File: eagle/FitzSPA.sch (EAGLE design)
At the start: 30 parts, among them U1 AD9200ARZ, U2 AD8129ARMZ, U3 VAT1-SMT

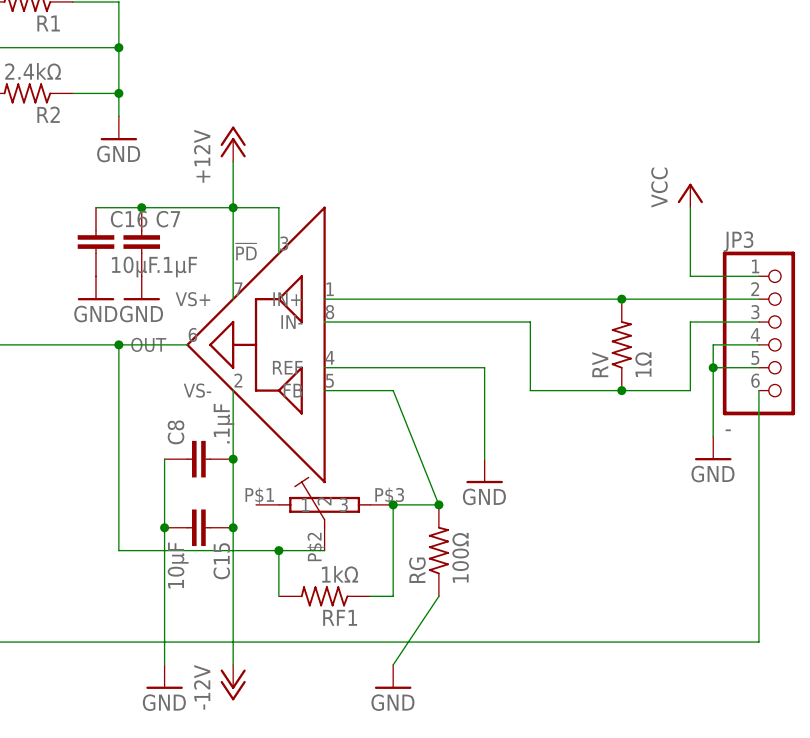
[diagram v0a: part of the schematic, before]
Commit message: Moving to branches for revisions instead of file names
changed filename
added 2nd POT on pin 4 of the diff amp to give a variable offset
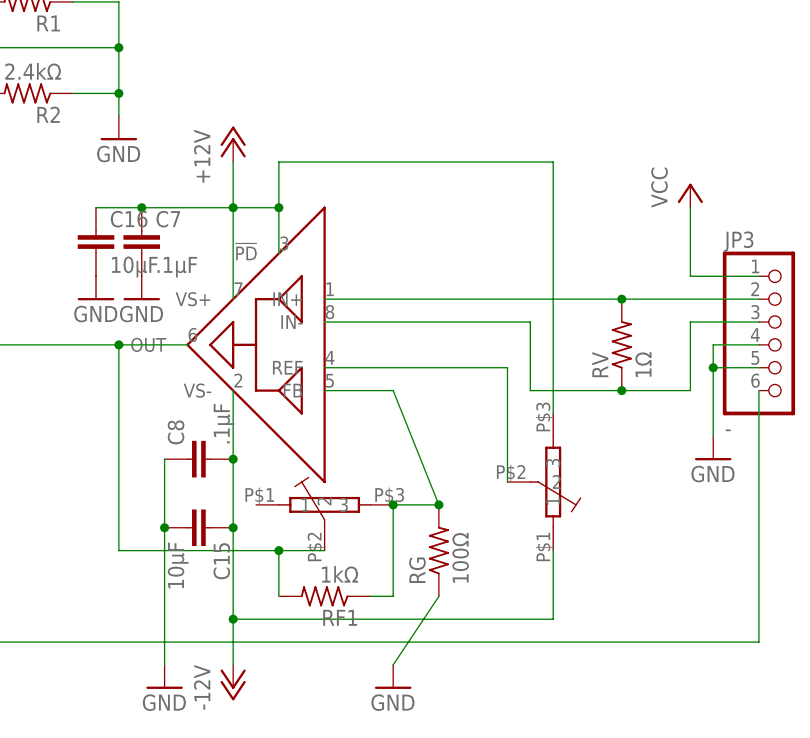
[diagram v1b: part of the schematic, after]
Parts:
- added RF2: 10kΩ, Model84POT:MODEL84POT
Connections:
- new net N$23: RF2.2, U2.REF
- net +12V: now also RF2.3
- net -12V: now also RF2.1
- net GND: no longer U2.REF
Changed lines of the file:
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@@
 <part name="P+2" library="supply1" deviceset="VCC" device=""/>
 <part name="GND1" library="supply1" deviceset="GND" device=""/>
-<part name="GND4" library="supply1" deviceset="GND" device=""/>
 <part name="GND6" library="supply1" deviceset="GND" device=""/>
 <part name="GND7" library="supply1" deviceset="GND" device=""/>
@@
 <part name="RF" library="Model84POT" deviceset="MODEL84POT" device="" value="10kΩ"/>
 <part name="RF1" library="rcl" deviceset="R-US_" device="R0603" value="1kΩ"/>
+<part name="RF2" library="Model84POT" deviceset="MODEL84POT" device="" value="10kΩ"/>
 </parts>
 <sheets>
@@
 <instance part="P+2" gate="VCC" x="-2.54" y="114.3"/>
 <instance part="GND1" gate="1" x="-5.08" y="53.34"/>
-<instance part="GND4" gate="1" x="137.16" y="76.2"/>
 <instance part="GND6" gate="1" x="93.98" y="96.52"/>
 <instance part="GND7" gate="1" x="127" y="53.34"/>
@@
 <instance part="RF" gate="G$1" x="119.38" y="73.66" rot="MR270"/>
 <instance part="RF1" gate="G$1" x="119.38" y="63.5" rot="R180"/>
+<instance part="RF2" gate="G$1" x="144.78" y="76.2" rot="R180"/>
 </instances>
 <busses>
@@
 <junction x="-5.08" y="68.58"/>
 <junction x="-12.7" y="68.58"/>
-</segment>
-<segment>
-<pinref part="GND4" gate="1" pin="GND"/>
-<pinref part="U2" gate="G$1" pin="REF"/>
-<wire x1="119.38" y1="88.9" x2="137.16" y2="88.9" width="0.1524" layer="91"/>
-<wire x1="137.16" y1="78.74" x2="137.16" y2="88.9" width="0.1524" layer="91"/>
 </segment>
 <segment>
@@
 <junction x="99.06" y="106.68"/>
 <pinref part="P+3" gate="1" pin="+12V"/>
+<wire x1="114.3" y1="106.68" x2="114.3" y2="111.76" width="0.1524" layer="91"/>
+<wire x1="114.3" y1="111.76" x2="144.78" y2="111.76" width="0.1524" layer="91"/>
+<junction x="114.3" y="106.68"/>
+<pinref part="RF2" gate="G$1" pin="3"/>
+<wire x1="144.78" y1="83.82" x2="144.78" y2="111.76" width="0.1524" layer="91"/>
 </segment>
 </net>
@@
 <pinref part="C15" gate="G$1" pin="1"/>
 <wire x1="109.22" y1="78.74" x2="109.22" y2="71.12" width="0.1524" layer="91"/>
-<wire x1="109.22" y1="71.12" x2="109.22" y2="55.88" width="0.1524" layer="91"/>
+<wire x1="109.22" y1="71.12" x2="109.22" y2="60.96" width="0.1524" layer="91"/>
 <junction x="109.22" y="71.12"/>
 <pinref part="C8" gate="G$1" pin="2"/>
 <junction x="109.22" y="78.74"/>
+<wire x1="109.22" y1="60.96" x2="109.22" y2="55.88" width="0.1524" layer="91"/>
+<wire x1="144.78" y1="60.96" x2="109.22" y2="60.96" width="0.1524" layer="91"/>
+<junction x="109.22" y="60.96"/>
+<pinref part="RF2" gate="G$1" pin="1"/>
+<wire x1="144.78" y1="60.96" x2="144.78" y2="68.58" width="0.1524" layer="91"/>
 </segment>
 </net>
@@
 </segment>
 </net>
+<net name="N$23" class="0">
+<segment>
+<pinref part="U2" gate="G$1" pin="REF"/>
+<wire x1="119.38" y1="88.9" x2="139.7" y2="88.9" width="0.1524" layer="91"/>
+<pinref part="RF2" gate="G$1" pin="2"/>
+<wire x1="139.7" y1="88.9" x2="139.7" y2="76.2" width="0.1524" layer="91"/>
+</segment>
+</net>
